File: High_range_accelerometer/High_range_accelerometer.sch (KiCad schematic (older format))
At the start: 55 parts, among them J1 USB_B_Micro, P1 KRC_PSoCWriter, U1 KRC_Conn_CAN, U2 NCP718ASN330T1G, U3 NCP718ASN500T1G, U4 NCV7342, U5 CY8C5868LTI-LP039, U6 H3LIS331DLTR, U7 W25N01GVxxIG-IT, Y2 Crystal_MHz

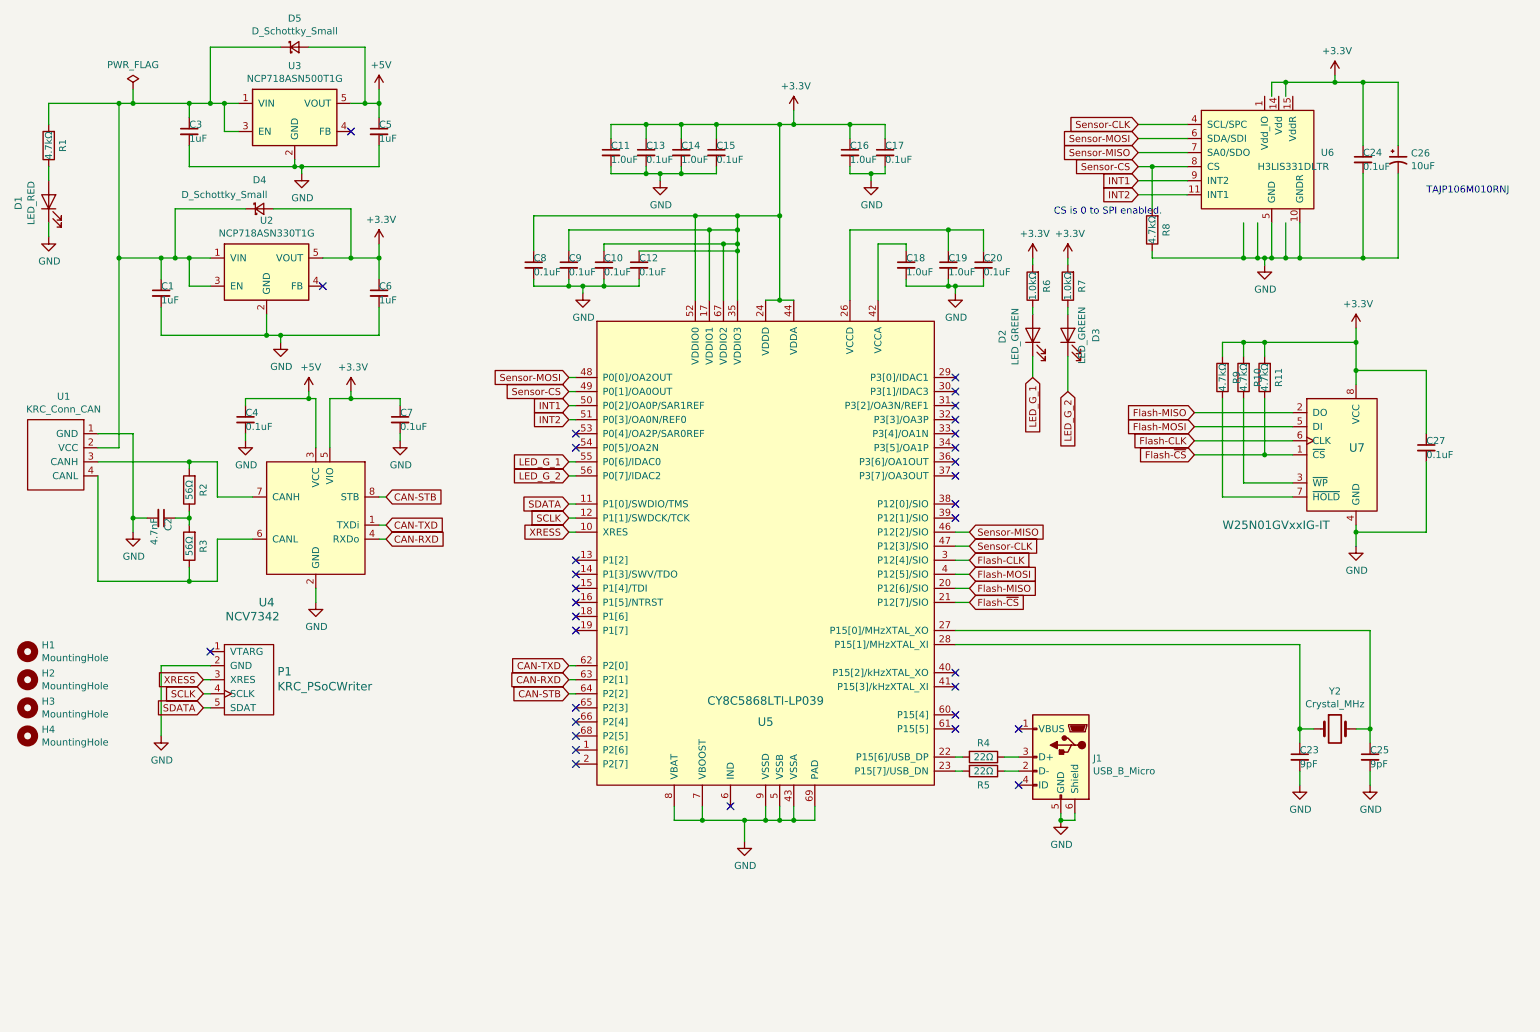
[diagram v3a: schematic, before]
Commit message: add sdCard
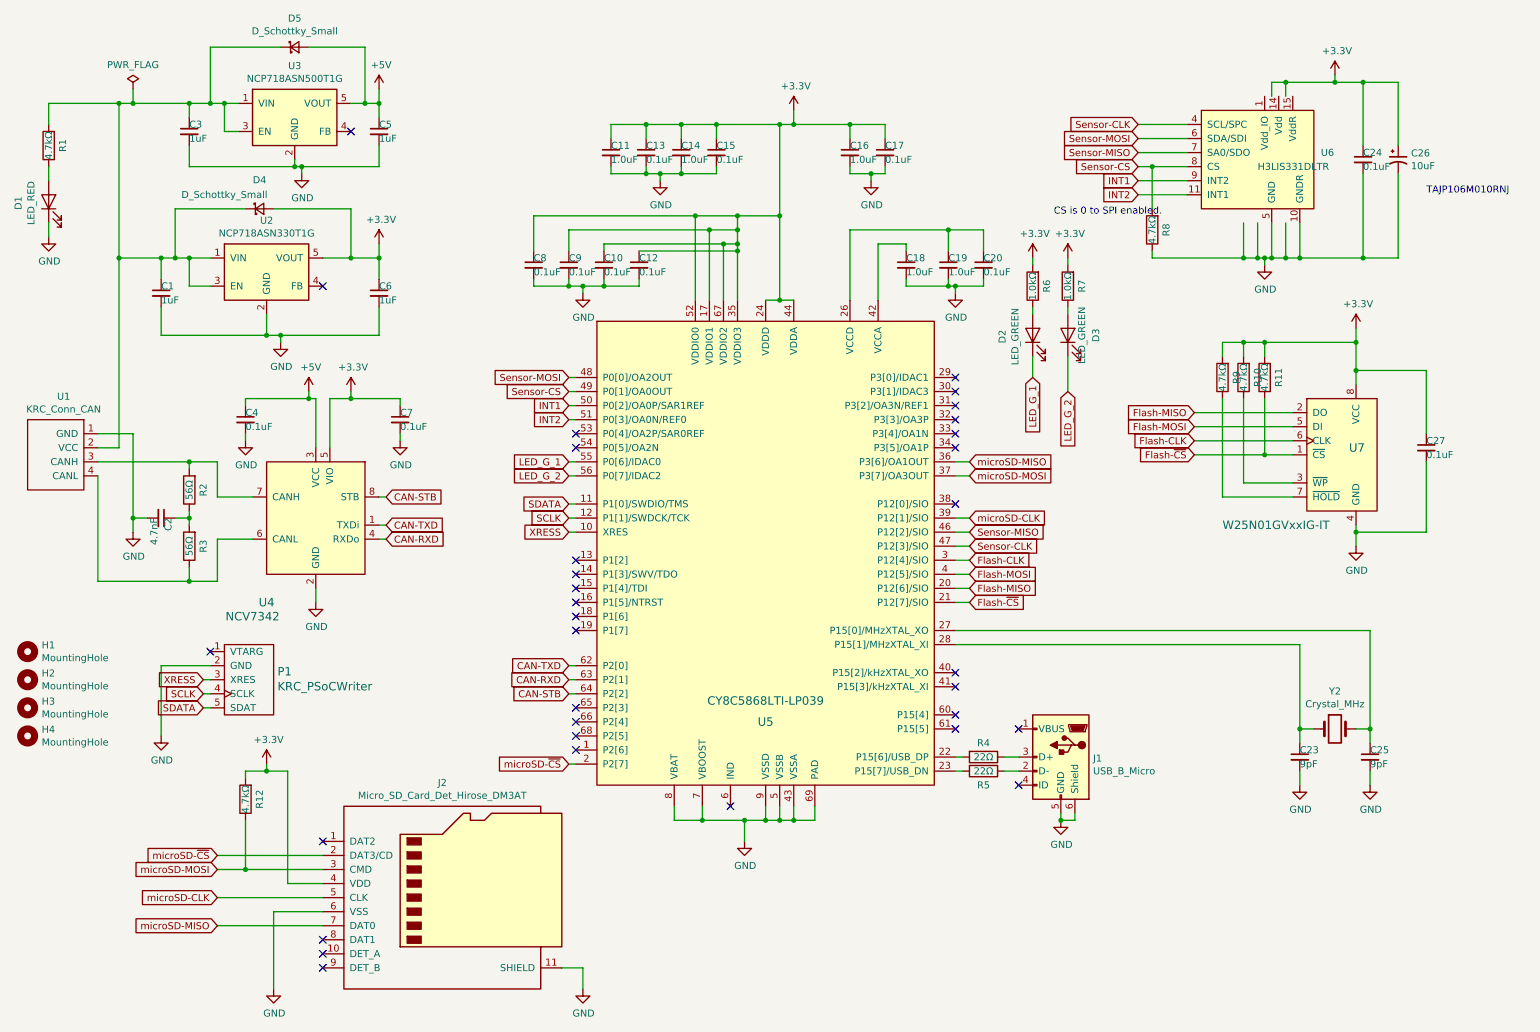
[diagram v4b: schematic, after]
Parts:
- added J2: Micro_SD_Card_Det_Hirose_DM3AT, Connector_Card:microSD_HC_Hirose_DM3AT-SF-PEJM5, symbol Connector:Micro_SD_Card_Det_Hirose_DM3AT
- added R12: 4.7kΩ, Resistor_SMD:R_0402_1005Metric, symbol Device:R
- R1: footprint Resistor_SMD:R_0603_1608Metric -> Resistor_SMD:R_0402_1005Metric
- R10, R11, R2, R3, R4, R5, R6, R7, R8, R9: footprint Capacitor_SMD:C_0402_1005Metric -> Resistor_SMD:R_0402_1005Metric
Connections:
- net +3V3: now also J2.4 (VDD), R12.2
- net GND: now also J2.11 (SHIELD), J2.6 (VSS)
- net microSD-~CS: now reaches U5.2 (P2[7])
- net microSD-~CS: now also J2.2 (DAT3/CD)
- net microSD-MISO: now reaches U5.36 (P3[6]/OA1OUT)
- net microSD-MISO: now also J2.7 (DAT0)
- net microSD-MOSI: now reaches U5.37 (P3[7]/OA3OUT)
- net microSD-MOSI: now also J2.3 (CMD), R12.1
- net microSD-CLK: now reaches U5.39 (P12[1]/SIO)
- net microSD-CLK: now also J2.5 (CLK)
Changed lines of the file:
@@
 F 0 "R4" V 7400 5750 50  0000 C CNN
 F 1 "22Ω" V 7500 5750 50  0000 C CNN
-F 2 "Capacitor_SMD:C_0402_1005Metric" V 7430 5750 50  0001 C CNN
+F 2 "Resistor_SMD:R_0402_1005Metric" V 7430 5750 50  0001 C CNN
 F 3 "~" H 7500 5750 50  0001 C CNN
 	1    7500 5750
@@
 F 0 "R5" V 7600 5850 50  0000 C CNN
 F 1 "22Ω" V 7500 5850 50  0000 C CNN
-F 2 "Capacitor_SMD:C_0402_1005Metric" V 7430 5850 50  0001 C CNN
+F 2 "Resistor_SMD:R_0402_1005Metric" V 7430 5850 50  0001 C CNN
 F 3 "~" H 7500 5850 50  0001 C CNN
 	1    7500 5850
@@
 F 0 "R11" V 9400 3050 50  0000 C CNN
 F 1 "4.7kΩ" V 9500 3050 50  0000 C CNN
-F 2 "Capacitor_SMD:C_0402_1005Metric" V 9430 3050 50  0001 C CNN
+F 2 "Resistor_SMD:R_0402_1005Metric" V 9430 3050 50  0001 C CNN
 F 3 "~" H 9500 3050 50  0001 C CNN
 	1    9500 3050
@@
 F 0 "R10" V 9250 3050 50  0000 C CNN
 F 1 "4.7kΩ" V 9350 3050 50  0000 C CNN
-F 2 "Capacitor_SMD:C_0402_1005Metric" V 9280 3050 50  0001 C CNN
+F 2 "Resistor_SMD:R_0402_1005Metric" V 9280 3050 50  0001 C CNN
 F 3 "~" H 9350 3050 50  0001 C CNN
 	1    9350 3050
@@
 F 0 "R9" V 9100 3050 50  0000 C CNN
 F 1 "4.7kΩ" V 9200 3050 50  0000 C CNN
-F 2 "Capacitor_SMD:C_0402_1005Metric" V 9130 3050 50  0001 C CNN
+F 2 "Resistor_SMD:R_0402_1005Metric" V 9130 3050 50  0001 C CNN
 F 3 "~" H 9200 3050 50  0001 C CNN
 	1    9200 3050
@@
 F 0 "R8" V 8600 2000 50  0000 C CNN
 F 1 "4.7kΩ" V 8700 2000 50  0000 C CNN
-F 2 "Capacitor_SMD:C_0402_1005Metric" V 8630 2000 50  0001 C CNN
+F 2 "Resistor_SMD:R_0402_1005Metric" V 8630 2000 50  0001 C CNN
 F 3 "~" H 8700 2000 50  0001 C CNN
 	1    8700 2000
@@
 F 0 "R2" V 1750 3850 50  0000 C CNN
 F 1 "56Ω" V 1850 3850 50  0000 C CNN
-F 2 "Capacitor_SMD:C_0402_1005Metric" V 1780 3850 50  0001 C CNN
+F 2 "Resistor_SMD:R_0402_1005Metric" V 1780 3850 50  0001 C CNN
 F 3 "~" H 1850 3850 50  0001 C CNN
 	1    1850 3850
@@
 F 0 "R3" V 1750 4250 50  0000 C CNN
 F 1 "56Ω" V 1850 4250 50  0000 C CNN
-F 2 "Capacitor_SMD:C_0402_1005Metric" V 1780 4250 50  0001 C CNN
+F 2 "Resistor_SMD:R_0402_1005Metric" V 1780 4250 50  0001 C CNN
 F 3 "~" H 1850 4250 50  0001 C CNN
 	1    1850 4250
@@
 F 0 "R1" V 750 1400 50  0000 C CNN
 F 1 "4.7kΩ" V 850 1400 50  0000 C CNN
-F 2 "Resistor_SMD:R_0603_1608Metric" V 780 1400 50  0001 C CNN
+F 2 "Resistor_SMD:R_0402_1005Metric" V 780 1400 50  0001 C CNN
 F 3 "~" H 850 1400 50  0001 C CNN
 	1    850  1400
@@
 F 0 "R6" V 7750 2400 50  0000 C CNN
 F 1 "1.0kΩ" V 7850 2400 50  0000 C CNN
-F 2 "Capacitor_SMD:C_0402_1005Metric" V 7780 2400 50  0001 C CNN
+F 2 "Resistor_SMD:R_0402_1005Metric" V 7780 2400 50  0001 C CNN
 F 3 "~" H 7850 2400 50  0001 C CNN
 	1    7850 2400
@@
 F 0 "R7" V 8000 2400 50  0000 C CNN
 F 1 "1.0kΩ" V 8100 2400 50  0000 C CNN
-F 2 "Capacitor_SMD:C_0402_1005Metric" V 8030 2400 50  0001 C CNN
+F 2 "Resistor_SMD:R_0402_1005Metric" V 8030 2400 50  0001 C CNN
 F 3 "~" H 8100 2400 50  0001 C CNN
 	1    8100 2400
@@
 NoConn ~ 7300 3450
 NoConn ~ 7300 3550
-NoConn ~ 7300 3650
-NoConn ~ 7300 3750
 NoConn ~ 7300 5450
 NoConn ~ 7300 5550
-NoConn ~ 4600 5800
 NoConn ~ 4600 5700
 NoConn ~ 4600 5600
@@
 $EndComp
 NoConn ~ 7300 3950
-NoConn ~ 7300 4050
 Wire Wire Line
 	4550 3350 4600 3350
@@
 NoConn ~ 7300 3050
 NoConn ~ 7300 3150
+$Comp
+L Connector:Micro_SD_Card_Det_Hirose_DM3AT J2
+U 1 1 5DA2CB78
+P 3700 6750
+F 0 "J2" H 3650 7567 50  0000 C CNN
+F 1 "Micro_SD_Card_Det_Hirose_DM3AT" H 3650 7476 50  0000 C CNN
+F 2 "Connector_Card:microSD_HC_Hirose_DM3AT-SF-PEJM5" H 5750 7450 50  0001 C CNN
+F 3 "https://www.hirose.com/product/en/download_file/key_name/DM3/category/Catalog/doc_file_id/49662/?file_category_id=4&item_id=195&is_series=1" H 3700 6850 50  0001 C CNN
+	1    3700 6750
+	1    0    0    -1
+$EndComp
+Wire Wire Line
+	4500 7250 4650 7250
+Wire Wire Line
+	4650 7250 4650 7400
+$Comp
+L power:GND #PWR030
+U 1 1 5DA436FA
+P 4650 7400
+F 0 "#PWR030" H 4650 7150 50  0001 C CNN
+F 1 "GND" H 4655 7227 50  0000 C CNN
+F 2 "" H 4650 7400 50  0001 C CNN
+F 3 "" H 4650 7400 50  0001 C CNN
+	1    4650 7400
+	1    0    0    -1
+$EndComp
+$Comp
+L Device:R R12
+U 1 1 5DA43ABD
+P 2250 6050
+F 0 "R12" V 2150 6050 50  0000 C CNN
+F 1 "4.7kΩ" V 2250 6050 50  0000 C CNN
+F 2 "Resistor_SMD:R_0402_1005Metric" V 2180 6050 50  0001 C CNN
+F 3 "~" H 2250 6050 50  0001 C CNN
+	1    2250 6050
+	-1   0    0    1
+$EndComp
+NoConn ~ 2800 6350
+NoConn ~ 2800 7150
+NoConn ~ 2800 7250
+NoConn ~ 2800 7050
+Text GLabel 2050 6950 0    50   Input ~ 0
+microSD-MISO
+Text GLabel 2050 6450 0    50   Input ~ 0
+microSD-~CS
+Text GLabel 2050 6550 0    50   Input ~ 0
+microSD-MOSI
+$Comp
+L power:+3.3V #PWR022
+U 1 1 5DA9F2CC
+P 2400 5800
+F 0 "#PWR022" H 2400 5650 50  0001 C CNN
+F 1 "+3.3V" H 2415 5973 50  0000 C CNN
+F 2 "" H 2400 5800 50  0001 C CNN
+F 3 "" H 2400 5800 50  0001 C CNN
+	1    2400 5800
+	1    0    0    -1
+$EndComp
+Wire Wire Line
+	2800 6850 2450 6850
+Wire Wire Line
+	2450 6850 2450 7400
+$Comp
+L power:GND #PWR023
+U 1 1 5DAB63A0
+P 2450 7400
+F 0 "#PWR023" H 2450 7150 50  0001 C CNN
+F 1 "GND" H 2455 7227 50  0000 C CNN
+F 2 "" H 2450 7400 50  0001 C CNN
+F 3 "" H 2450 7400 50  0001 C CNN
+	1    2450 7400
+	1    0    0    -1
+$EndComp
+Text GLabel 2050 6750 0    50   Input ~ 0
+microSD-CLK
+Wire Wire Line
+	2800 6650 2550 6650
+Wire Wire Line
+	2550 6650 2550 5850
+Wire Wire Line
+	2550 5850 2400 5850
+Wire Wire Line
+	2250 5850 2250 5900
+Wire Wire Line
+	2400 5800 2400 5850
+Connection ~ 2400 5850
+Wire Wire Line
+	2400 5850 2250 5850
+Wire Wire Line
+	2250 6200 2250 6550
+Wire Wire Line
+	2250 6550 2800 6550
+Wire Wire Line
+	2050 6450 2800 6450
+Wire Wire Line
+	2250 6550 2050 6550
+Connection ~ 2250 6550
+Wire Wire Line
+	2050 6750 2800 6750
+Wire Wire Line
+	2800 6950 2050 6950
+Text GLabel 7400 3650 2    50   Input ~ 0
+microSD-MISO
+Text GLabel 4550 5800 0    50   Input ~ 0
+microSD-~CS
+Text GLabel 7400 3750 2    50   Input ~ 0
+microSD-MOSI
+Text GLabel 7400 4050 2    50   Input ~ 0
+microSD-CLK
+Wire Wire Line
+	4600 5800 4550 5800
+Wire Wire Line
+	7400 4050 7300 4050
+Wire Wire Line
+	7300 3750 7400 3750
+Wire Wire Line
+	7400 3650 7300 3650
 $EndSCHEMATC

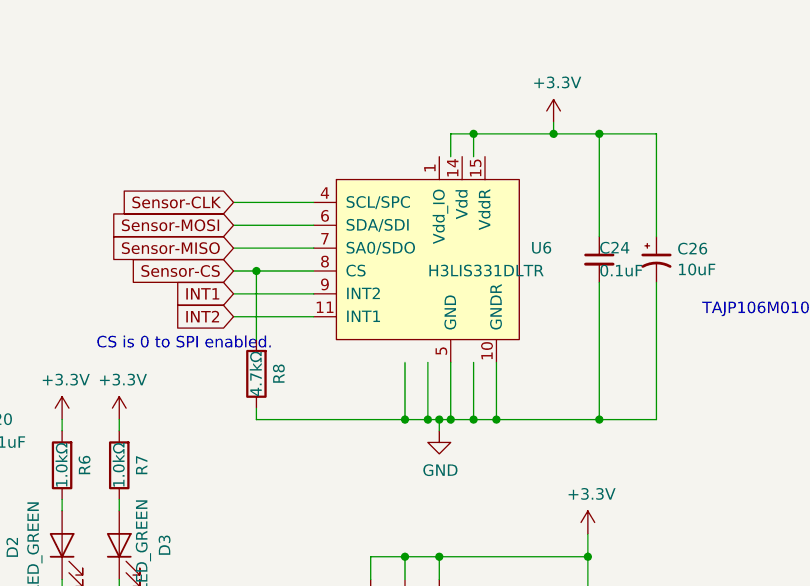
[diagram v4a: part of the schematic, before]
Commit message: modified sensor footprint
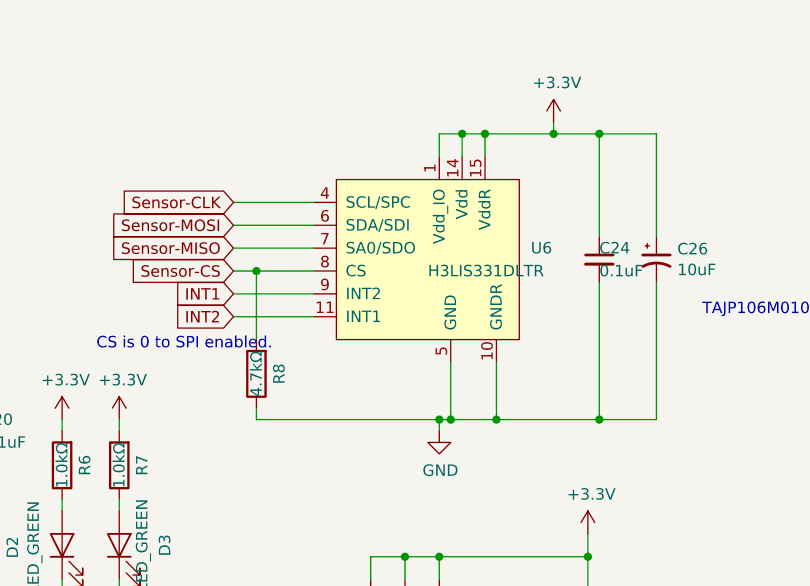
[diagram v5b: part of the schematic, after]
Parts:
- U6: footprint Package_LGA:LGA-16_3x3mm_P0.5mm_LayoutBorder3x5y -> my_footprint:LGA-16_3x3mm_P0.5mm_LayoutBorder3x5y_handsoldering
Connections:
- net +3V3: now also U6.1 (Vdd_IO), U6.14 (Vdd), U6.15 (VddR)
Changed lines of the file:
@@
 	8700 2200 8700 2150
 Wire Wire Line
-	9350 1950 9350 2200
-Connection ~ 9350 2200
-Wire Wire Line
-	9350 2200 8700 2200
-Wire Wire Line
 	9500 2250 9500 2200
-Wire Wire Line
-	9350 2200 9450 2200
-Wire Wire Line
-	9450 1950 9450 2200
-Connection ~ 9450 2200
-Wire Wire Line
-	9450 2200 9500 2200
 Wire Wire Line
 	9550 1950 9550 2200
@@
 	9550 2200 9500 2200
 Connection ~ 9500 2200
-Wire Wire Line
-	9550 2200 9650 2200
-Wire Wire Line
-	9650 2200 9650 1950
 Connection ~ 9550 2200
 Wire Wire Line
 	9750 1950 9750 2200
 Wire Wire Line
-	9750 2200 9650 2200
-Connection ~ 9650 2200
-Wire Wire Line
-	9550 1050 9550 950
-Wire Wire Line
-	9550 950  9650 950
-Wire Wire Line
 	10000 950  10000 900
-Wire Wire Line
-	9650 1050 9650 950
-Connection ~ 9650 950
-Wire Wire Line
-	9650 950  10000 950
 Wire Wire Line
 	10000 950  10200 950
@@
 F 0 "U6" H 9900 1550 50  0000 L CNN
 F 1 "H3LIS331DLTR" H 9450 1450 50  0000 L CNN
-F 2 "Package_LGA:LGA-16_3x3mm_P0.5mm_LayoutBorder3x5y" H 9400 900 50  0001 C CNN
+F 2 "my_footprint:LGA-16_3x3mm_P0.5mm_LayoutBorder3x5y_handsoldering" H 9400 900 50  0001 C CNN
 F 3 "https://www.st.com/content/ccc/resource/technical/document/datasheet/3e/48/02/c7/a4/e6/41/bb/DM00053090.pdf/files/DM00053090.pdf/jcr:content/translations/en.DM00053090.pdf" H 11200 900 50  0001 C CNN
 	1    9450 1500
@@
 Wire Wire Line
 	7400 3650 7300 3650
+Wire Wire Line
+	9700 1050 9700 950
+Connection ~ 9700 950
+Wire Wire Line
+	9700 950  10000 950
+Wire Wire Line
+	9500 1050 9500 950
+Wire Wire Line
+	9500 950  9600 950
+Wire Wire Line
+	9600 1050 9600 950
+Connection ~ 9600 950
+Wire Wire Line
+	9600 950  9700 950
+Wire Wire Line
+	8700 2200 9500 2200
+Wire Wire Line
+	9550 2200 9750 2200
 $EndSCHEMATC
